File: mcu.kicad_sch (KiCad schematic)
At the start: 6 parts, among them U1 STM32G071KBU6

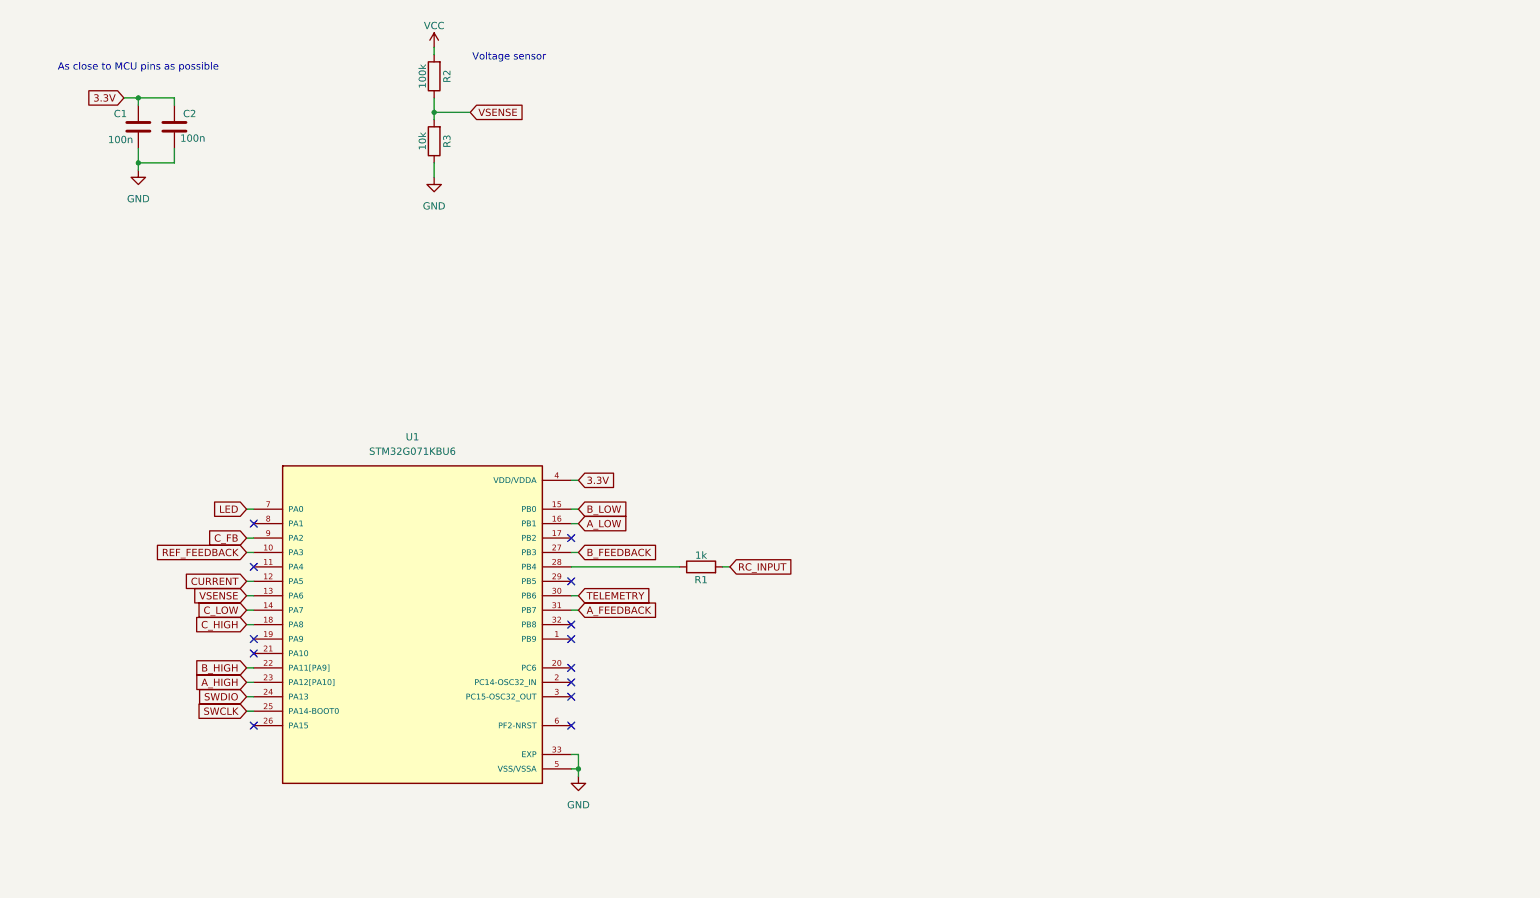
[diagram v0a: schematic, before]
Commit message: finished one full channel, still to duplicate this for 4 channels esc
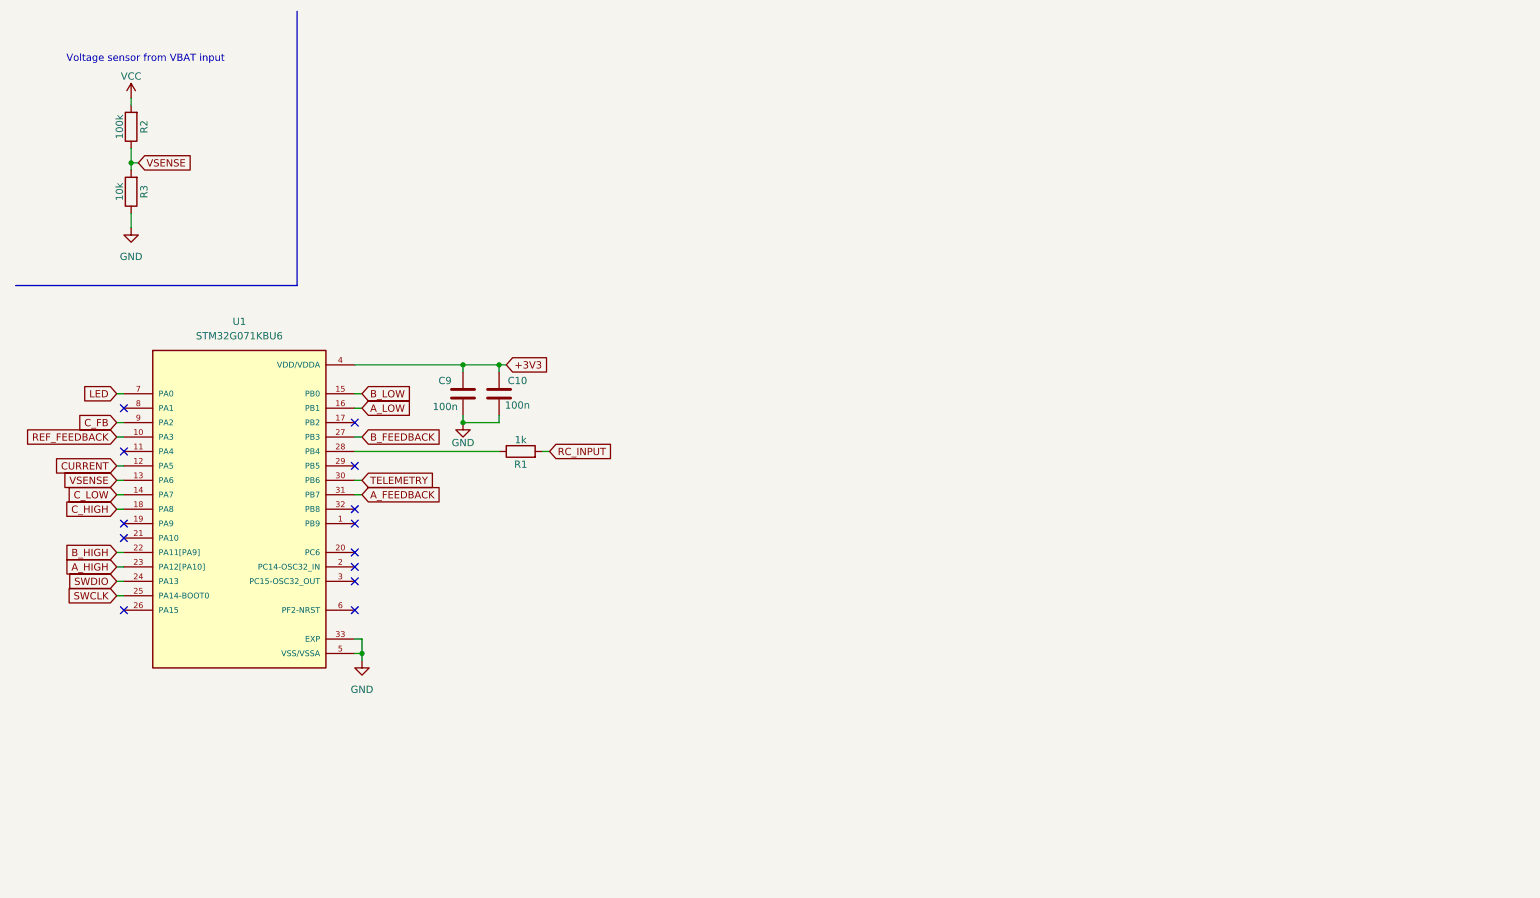
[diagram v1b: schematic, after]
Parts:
- removed C1, C2: 100n, symbol Device:C
- added C10, C9: 100n, symbol Device:C
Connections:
- net GND: now also C10.2, C9.2
- net 3.3V renamed +3V3
- net +3V3: now also C10.1, C9.1
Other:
- note added: "Voltage sensor from VBAT input"
- note removed: "As close to MCU pins as possible"
- note removed: "Voltage sensor"
- moved on the sheet: R1, R2, R3, U1

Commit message: duplicate mcu and motor gates circuit
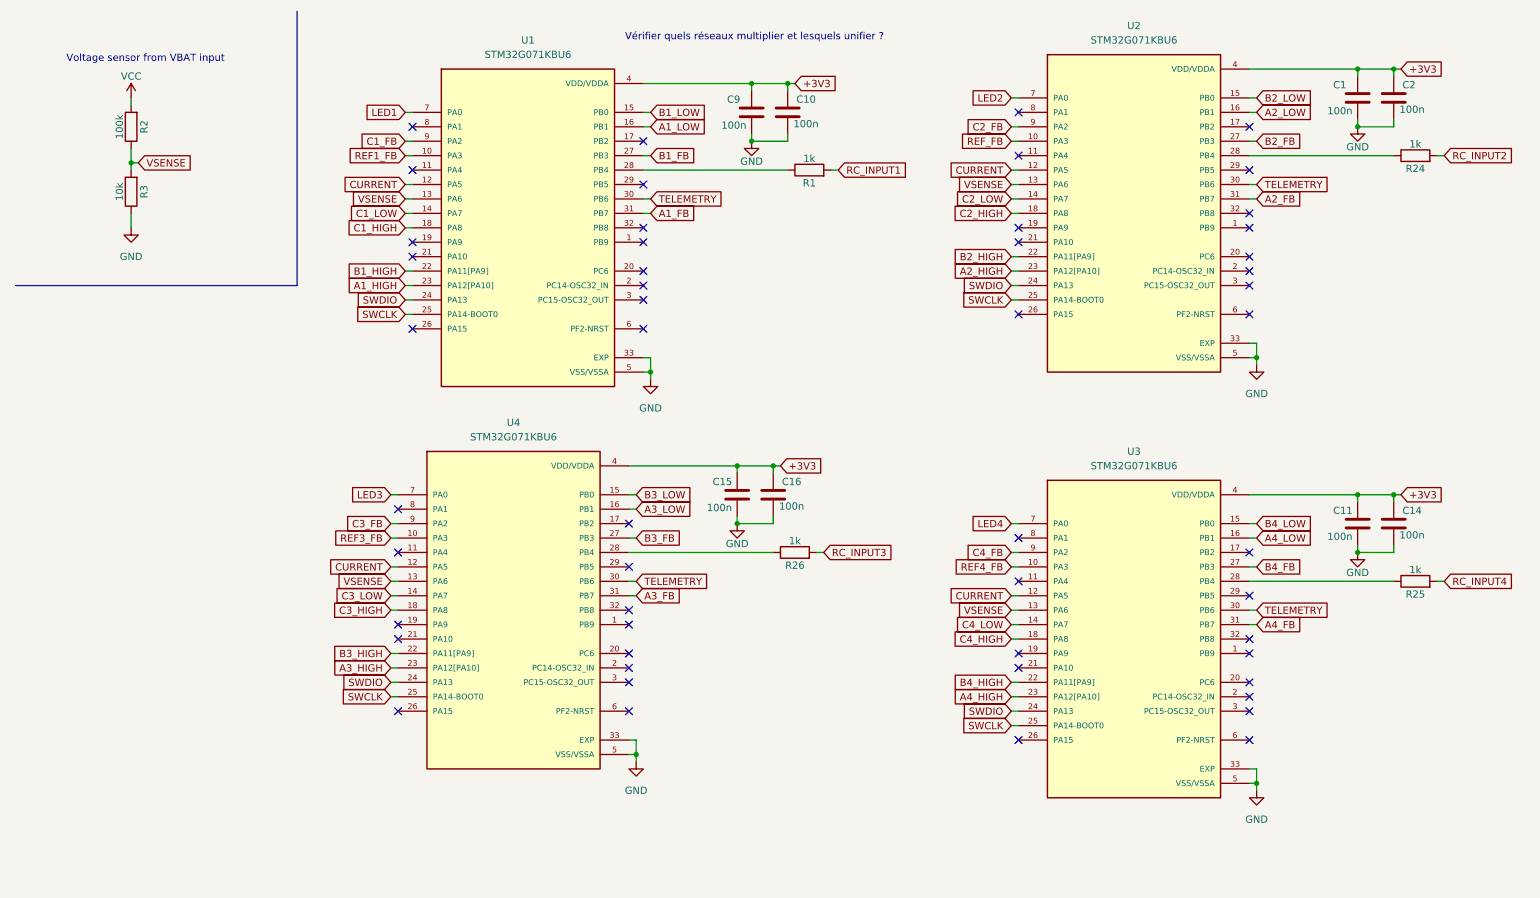
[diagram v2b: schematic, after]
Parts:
- added C1, C11, C14, C15, C16, C2: 100n, symbol Device:C
- added R24, R25, R26: 1k, symbol Device:R
- added U2, U3, U4: STM32G071KBU6, ESCs:QFN50P500X500X60-33N, symbol ESCs:STM32G071KBU6
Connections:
- net +3V3: now also C1.1, C11.1, C14.1, C15.1, C16.1, C2.1, U2.4 (VDD/VDDA), U3.4 (VDD/VDDA), U4.4 (VDD/VDDA)
- net CURRENT: now also U2.12 (PA5), U3.12 (PA5), U4.12 (PA5)
- net GND: now also C1.2, C11.2, C14.2, C15.2, C16.2, C2.2, U2.33 (EXP), U2.5 (VSS/VSSA), U3.33 (EXP), U3.5 (VSS/VSSA), U4.33 (EXP), U4.5 (VSS/VSSA)
- net SWCLK: now also U2.25 (PA14-BOOT0), U3.25 (PA14-BOOT0), U4.25 (PA14-BOOT0)
- net SWDIO: now also U2.24 (PA13), U3.24 (PA13), U4.24 (PA13)
- net TELEMETRY: now also U2.30 (PB6), U3.30 (PB6), U4.30 (PB6)
- net VSENSE: now also U2.13 (PA6), U3.13 (PA6), U4.13 (PA6)
- net A_FEEDBACK renamed A1_FB
- net A_HIGH renamed A1_HIGH
- net A_LOW renamed A1_LOW
- net B_FEEDBACK renamed B1_FB
- net B_HIGH renamed B1_HIGH
- net B_LOW renamed B1_LOW
- net C_FB renamed C1_FB
- net C_HIGH renamed C1_HIGH
- net C_LOW renamed C1_LOW
- net LED renamed LED1
- net RC_INPUT renamed RC_INPUT1
- net REF_FEEDBACK renamed REF1_FB
- new net: R25.1, U3.28 (PB4)
- new net: R24.1, U2.28 (PB4)
- new net: R26.1, U4.28 (PB4)
- new net A2_FB: U2.31 (PB7)
- new net A2_HIGH: U2.23 (PA12[PA10])
- new net A2_LOW: U2.16 (PB1)
- new net A3_FB: U4.31 (PB7)
- new net A3_HIGH: U4.23 (PA12[PA10])
- new net A3_LOW: U4.16 (PB1)
- new net A4_FB: U3.31 (PB7)
- new net A4_HIGH: U3.23 (PA12[PA10])
- new net A4_LOW: U3.16 (PB1)
- new net B2_FB: U2.27 (PB3)
- new net B2_HIGH: U2.22 (PA11[PA9])
- new net B2_LOW: U2.15 (PB0)
- new net B3_FB: U4.27 (PB3)
- new net B3_HIGH: U4.22 (PA11[PA9])
- new net B3_LOW: U4.15 (PB0)
- new net B4_FB: U3.27 (PB3)
- new net B4_HIGH: U3.22 (PA11[PA9])
- new net B4_LOW: U3.15 (PB0)
- new net C2_FB: U2.9 (PA2)
- new net C2_HIGH: U2.18 (PA8)
- new net C2_LOW: U2.14 (PA7)
- new net C3_FB: U4.9 (PA2)
- new net C3_HIGH: U4.18 (PA8)
- new net C3_LOW: U4.14 (PA7)
- new net C4_FB: U3.9 (PA2)
- new net C4_HIGH: U3.18 (PA8)
- new net C4_LOW: U3.14 (PA7)
- new net LED2: U2.7 (PA0)
- new net LED3: U4.7 (PA0)
- new net LED4: U3.7 (PA0)
- new net RC_INPUT2: R24.2
- new net RC_INPUT3: R26.2
- new net RC_INPUT4: R25.2
- new net REF3_FB: U4.10 (PA3)
- new net REF4_FB: U3.10 (PA3)
- new net REF_FB: U2.10 (PA3)
- no-connect marks 13 -> 52
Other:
- note added: "Vérifier quels réseaux multiplier et lesquels unifier ?"
- moved on the sheet: C10, C9, R1, U1

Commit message: update schematic
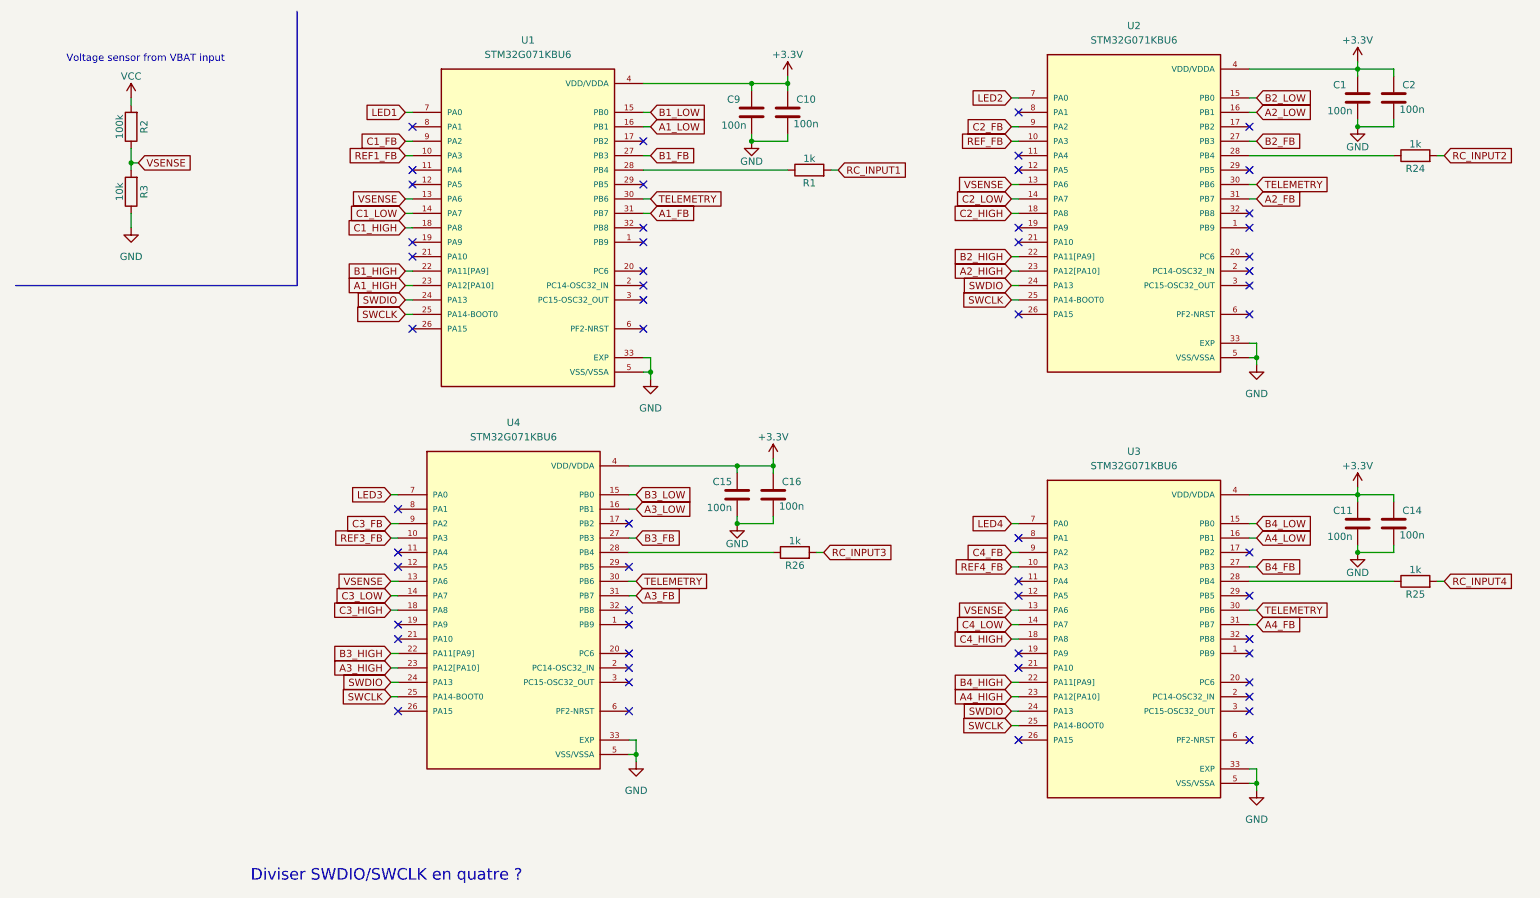
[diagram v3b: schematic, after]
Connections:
- net +3V3 renamed +3.3V
- removed net CURRENT: U1.12 (PA5), U2.12 (PA5), U3.12 (PA5), U4.12 (PA5)
- no-connect marks 52 -> 56
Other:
- note added: "Diviser SWDIO/SWCLK en quatre ?"
- note removed: "Vérifier quels réseaux multiplier et lesquels unifier ?"

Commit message: affected footprints
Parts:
- C1, C10, C11, C14, C15, C16, C2, C9: value 100n -> 0.1u; footprint (none) -> Capacitor_SMD:C_0402_1005Metric
- R1, R2, R24, R25, R26, R3: footprint (none) -> Resistor_SMD:R_0402_1005Metric
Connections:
- removed net SWCLK: U1.25 (PA14-BOOT0), U2.25 (PA14-BOOT0), U3.25 (PA14-BOOT0), U4.25 (PA14-BOOT0)
- removed net SWDIO: U1.24 (PA13), U2.24 (PA13), U3.24 (PA13), U4.24 (PA13)
- new net SWCLK1: U1.25 (PA14-BOOT0)
- new net SWCLK2: U2.25 (PA14-BOOT0)
- new net SWCLK3: U4.25 (PA14-BOOT0)
- new net SWCLK4: U3.25 (PA14-BOOT0)
- new net SWDIO1: U1.24 (PA13)
- new net SWDIO2: U2.24 (PA13)
- new net SWDIO3: U4.24 (PA13)
- new net SWDIO4: U3.24 (PA13)
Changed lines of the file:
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@@
 		)
 	)
-	(global_label "SWCLK"
+	(global_label "SWCLK2"
 		(shape input)
 		(at 187.96 63.5 180)
@@
 		)
 		(property "Intersheetrefs" "${INTERSHEET_REFS}"
-			(at 178.7458 63.5 0)
+			(at 177.5363 63.5 0)
 			(effects
 				(font
@@
 		)
 	)
-	(global_label "SWCLK"
+	(global_label "SWCLK3"
 		(shape input)
 		(at 78.74 133.35 180)
@@
 		)
 		(property "Intersheetrefs" "${INTERSHEET_REFS}"
-			(at 69.5258 133.35 0)
+			(at 68.3163 133.35 0)
 			(effects
 				(font
@@
 		)
 	)
-	(global_label "SWDIO"
+	(global_label "SWDIO2"
 		(shape input)
 		(at 187.96 60.96 180)
@@
 		)
 		(property "Intersheetrefs" "${INTERSHEET_REFS}"
-			(at 179.1086 60.96 0)
+			(at 177.8991 60.96 0)
 			(effects
 				(font
@@
 		)
 	)
-	(global_label "SWDIO"
+	(global_label "SWDIO4"
 		(shape input)
 		(at 187.96 135.89 180)
@@
 		)
 		(property "Intersheetrefs" "${INTERSHEET_REFS}"
-			(at 179.1086 135.89 0)
+			(at 177.8991 135.89 0)
 			(effects
 				(font
@@
 		)
 	)
-	(global_label "SWDIO"
+	(global_label "SWDIO3"
 		(shape input)
 		(at 78.74 130.81 180)
@@
 		)
 		(property "Intersheetrefs" "${INTERSHEET_REFS}"
-			(at 69.8886 130.81 0)
+			(at 68.6791 130.81 0)
 			(effects
 				(font
@@
 		)
 	)
-	(global_label "SWDIO"
+	(global_label "SWDIO1"
 		(shape input)
 		(at 81.28 63.5 180)
@@
 		)
 		(property "Intersheetrefs" "${INTERSHEET_REFS}"
-			(at 72.4286 63.5 0)
+			(at 71.2191 63.5 0)
 			(effects
 				(font
@@
 		)
 	)
-	(global_label "SWCLK"
+	(global_label "SWCLK1"
 		(shape input)
 		(at 81.28 66.04 180)
@@
 		)
 		(property "Intersheetrefs" "${INTERSHEET_REFS}"
-			(at 72.0658 66.04 0)
+			(at 70.8563 66.04 0)
 			(effects
 				(font
@@
 		)
 	)
-	(global_label "SWCLK"
+	(global_label "SWCLK4"
 		(shape input)
 		(at 187.96 138.43 180)
@@
 		)
 		(property "Intersheetrefs" "${INTERSHEET_REFS}"
-			(at 178.7458 138.43 0)
+			(at 177.5363 138.43 0)
 			(effects
 				(font
@@
 			)
 		)
-		(property "Footprint" ""
+		(property "Footprint" "Resistor_SMD:R_0402_1005Metric"
 			(at 34.798 33.02 90)
 			(effects
@@
 			)
 		)
-		(property "Footprint" ""
+		(property "Footprint" "Resistor_SMD:R_0402_1005Metric"
 			(at 34.798 44.45 90)
 			(effects
@@
 			)
 		)
-		(property "Value" "100n"
+		(property "Value" "0.1u"
 			(at 136.906 32.766 0)
 			(effects
@@
 			)
 		)
-		(property "Footprint" ""
+		(property "Footprint" "Capacitor_SMD:C_0402_1005Metric"
 			(at 143.2052 34.29 0)
 			(effects
@@
 			)
 		)
-		(property "Value" "100n"
+		(property "Value" "0.1u"
 			(at 147.066 99.822 0)
 			(effects
@@
 			)
 		)
-		(property "Footprint" ""
+		(property "Footprint" "Capacitor_SMD:C_0402_1005Metric"
 			(at 147.0152 101.6 0)
 			(effects
@@
 			)
 		)
-		(property "Value" "100n"
+		(property "Value" "0.1u"
 			(at 134.366 100.076 0)
 			(effects
@@
 			)
 		)
-		(property "Footprint" ""
+		(property "Footprint" "Capacitor_SMD:C_0402_1005Metric"
 			(at 140.6652 101.6 0)
 			(effects
@@
 			)
 		)
-		(property "Value" "100n"
+		(property "Value" "0.1u"
 			(at 256.286 104.902 0)
 			(effects
@@
 			)
 		)
-		(property "Footprint" ""
+		(property "Footprint" "Capacitor_SMD:C_0402_1005Metric"
 			(at 256.2352 106.68 0)
 			(effects
@@
 			)
 		)
-		(property "Footprint" ""
+		(property "Footprint" "Resistor_SMD:R_0402_1005Metric"
 			(at 152.4 42.418 90)
 			(effects
@@
 			)
 		)
-		(property "Value" "100n"
+		(property "Value" "0.1u"
 			(at 149.606 32.512 0)
 			(effects
@@
 			)
 		)
-		(property "Footprint" ""
+		(property "Footprint" "Capacitor_SMD:C_0402_1005Metric"
 			(at 149.5552 34.29 0)
 			(effects
@@
 			)
 		)
-		(property "Value" "100n"
+		(property "Value" "0.1u"
 			(at 256.286 29.972 0)
 			(effects
@@
 			)
 		)
-		(property "Footprint" ""
+		(property "Footprint" "Capacitor_SMD:C_0402_1005Metric"
 			(at 256.2352 31.75 0)
 			(effects
@@
 			)
 		)
-		(property "Footprint" ""
+		(property "Footprint" "Resistor_SMD:R_0402_1005Metric"
 			(at 149.86 109.728 90)
 			(effects
@@
 			)
 		)
-		(property "Footprint" ""
+		(property "Footprint" "Resistor_SMD:R_0402_1005Metric"
 			(at 259.08 39.878 90)
 			(effects
@@
 			)
 		)
-		(property "Value" "100n"
+		(property "Value" "0.1u"
 			(at 243.586 105.156 0)
 			(effects
@@
 			)
 		)
-		(property "Footprint" ""
+		(property "Footprint" "Capacitor_SMD:C_0402_1005Metric"
 			(at 249.8852 106.68 0)
 			(effects
@@
 			)
 		)
-		(property "Value" "100n"
+		(property "Value" "0.1u"
 			(at 243.586 30.226 0)
 			(effects
@@
 			)
 		)
-		(property "Footprint" ""
+		(property "Footprint" "Capacitor_SMD:C_0402_1005Metric"
 			(at 249.8852 31.75 0)
 			(effects
@@
 			)
 		)
-		(property "Footprint" ""
+		(property "Footprint" "Resistor_SMD:R_0402_1005Metric"
 			(at 259.08 114.808 90)
 			(effects
